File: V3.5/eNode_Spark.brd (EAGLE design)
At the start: 30 x 65 mm, 80 parts, among them Q1 MOSFET-PCHANNEL_SOT23-3, U1 WM-N-BM-09, U10 OPA344, U2 MCP73831T-2ACI/OT, U3 R8008-33, U5 HTU21DSMD, U6 TMP006, U7 BMP180, U8 USD-SOCKETSMD, U9 MIC9.7MM

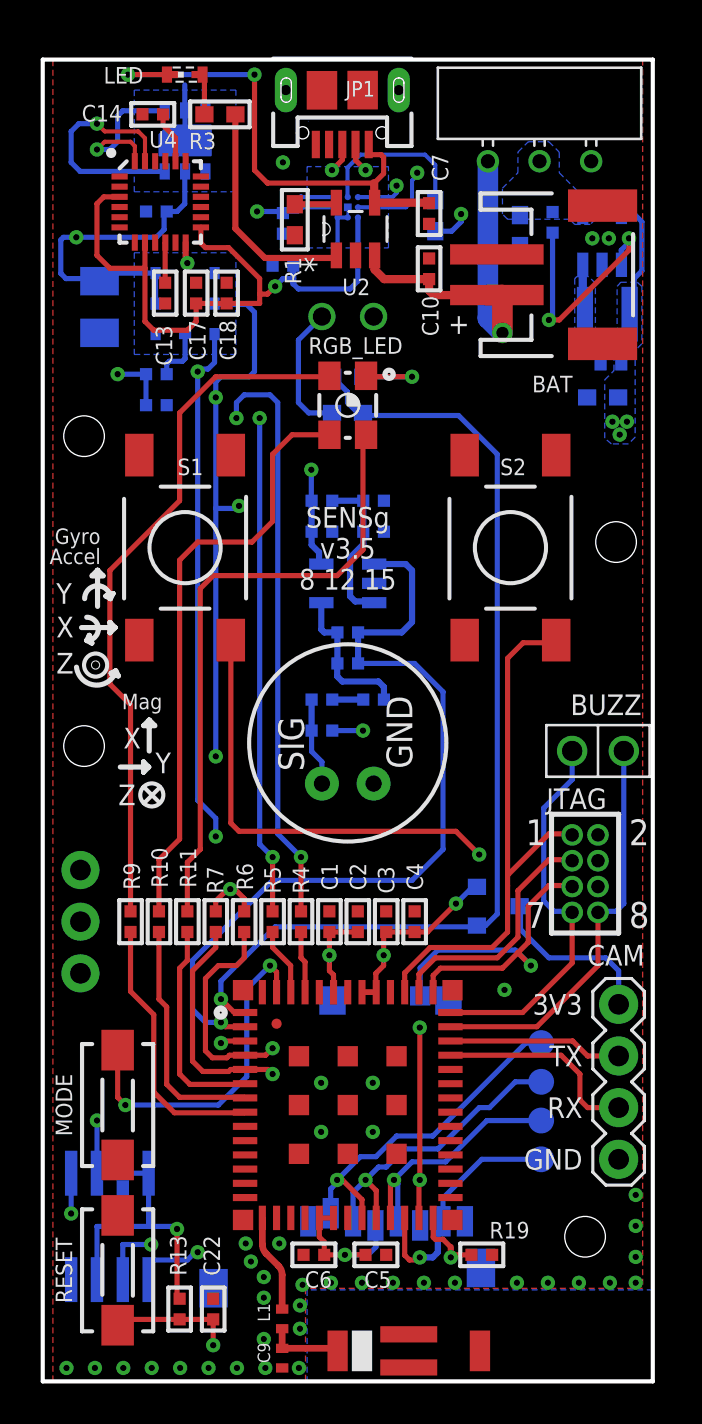
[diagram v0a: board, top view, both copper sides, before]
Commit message: Changed to Micro USB B.lbr
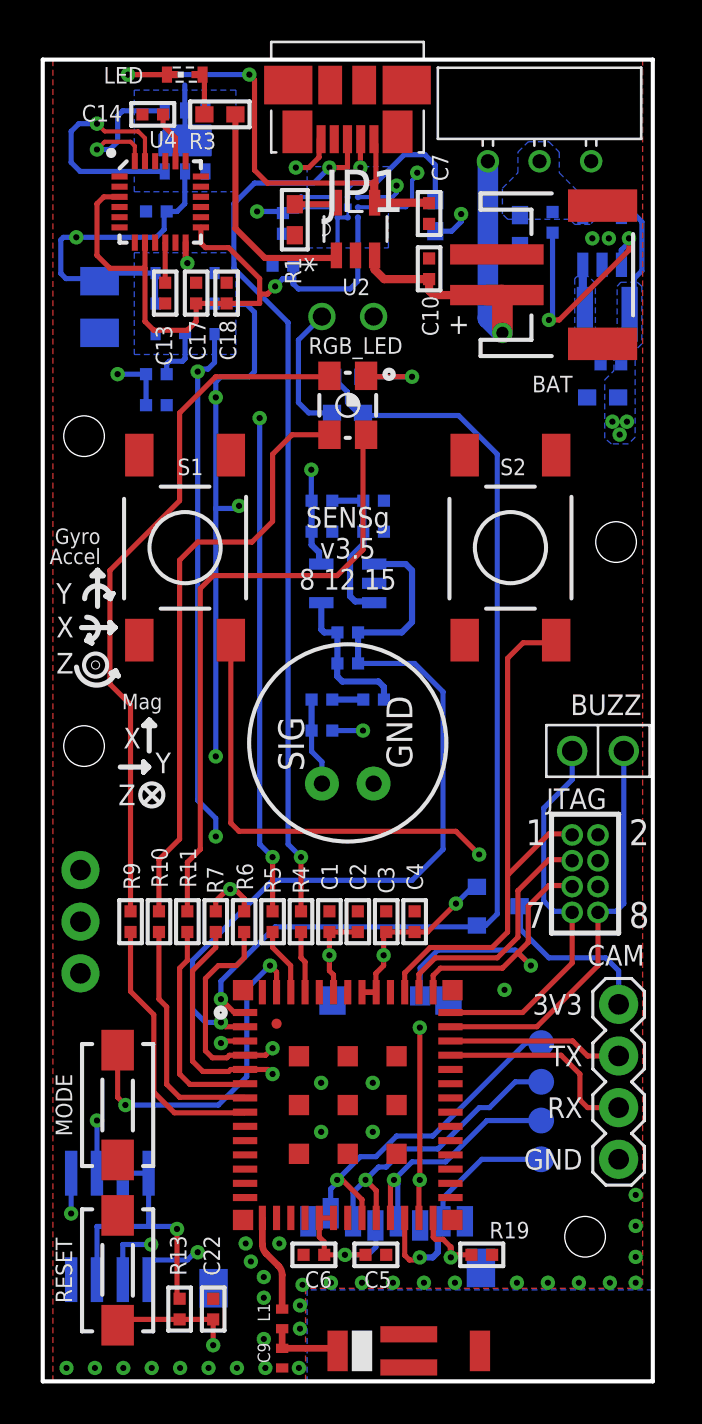
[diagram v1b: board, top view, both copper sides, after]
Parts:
- JP1: value USBUSB-MICROB-SLOT-HOLE -> (none); device Spark:USB-MICROB-SLOT-HOLE -> Micro USB B:MOLEX_47346-0001
- moved JP1 2.43 mm to (15.0, 61.1)
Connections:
- removed net MF: JP1.D+, R4.2
- new net N$17: JP1.3, R4.2
- net GND: now also JP1.5; no longer JP1.GND, JP1.MT1, JP1.MT2
- net N$18: now also JP1.2; no longer JP1.D-
- net UVCC: now also JP1.1; no longer JP1.VBUS
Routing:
- net MF: track 46.3 -> 0.00 mm, vias 3 -> 0
- net N$17: track 0.00 -> 43.9 mm, vias 0 -> 2
- net GND: track 9.57 -> 11.8 mm
- net N$25: track 7.98 -> 7.39 mm
- net N$18: track 41.8 -> 41.3 mm
